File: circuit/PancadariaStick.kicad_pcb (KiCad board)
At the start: 2 copper layers, 64.8 x 63.5 mm, 21 parts, among them CON1 AVR-ISP-10, IC1 ATMEGA8-P, P1 Joystick, P2 Buttons, P3 USB type B, Q1 16MHz

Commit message: Fixed "jumper vias" drill size.
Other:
- net class Default: via_drill 1 -> 0.8
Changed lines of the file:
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@@
     (edge_width 0.15)
     (via_size 2)
-    (via_drill 1)
+    (via_drill 0.8)
     (via_min_size 0.4)
     (via_min_drill 0.3)
@@
       (drillshape 0)
       (scaleselection 1)
-      (outputdirectory curtacircuitos/))
+      (outputdirectory test/))
   )
   (net 0 "")
@@
     (trace_width 0.3)
     (via_dia 2)
-    (via_drill 1)
+    (via_drill 0.8)
     (uvia_dia 0.3)
     (uvia_drill 0.1)

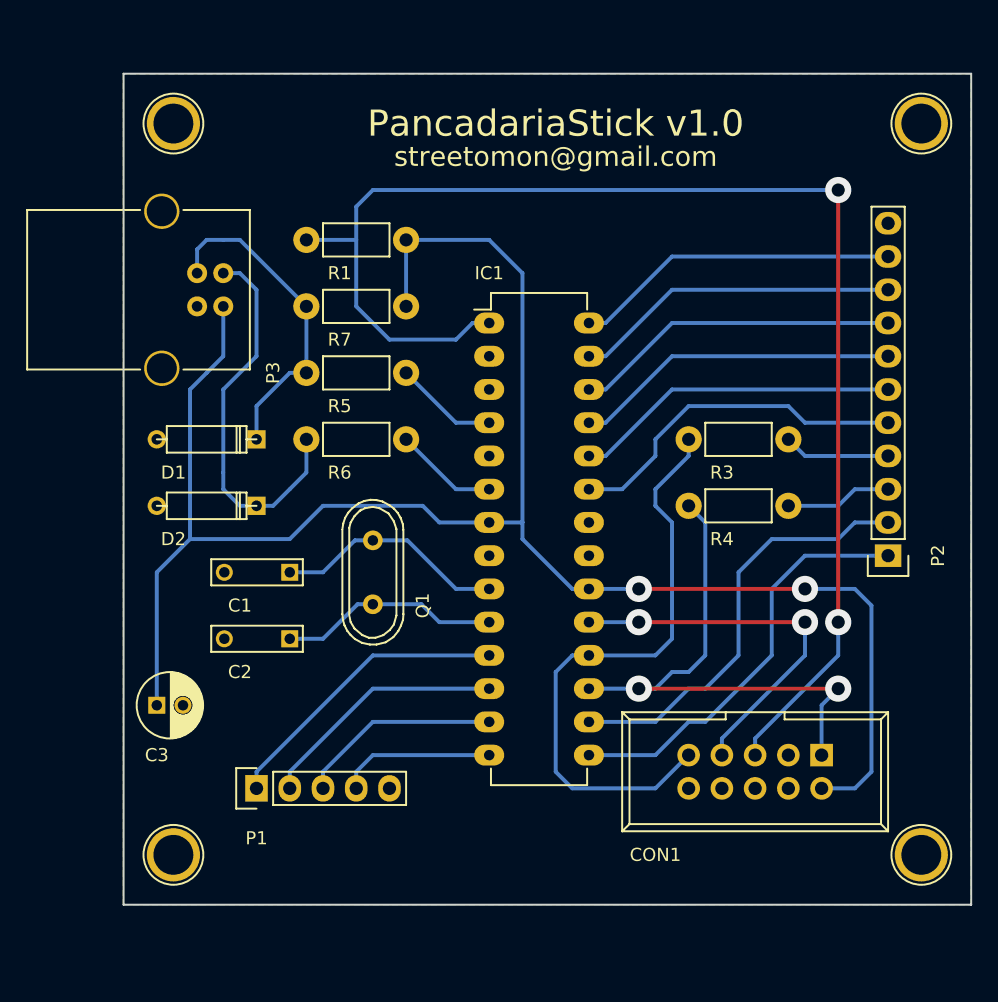
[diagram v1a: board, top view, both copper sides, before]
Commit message: Changed traces width to 0.8 mm.
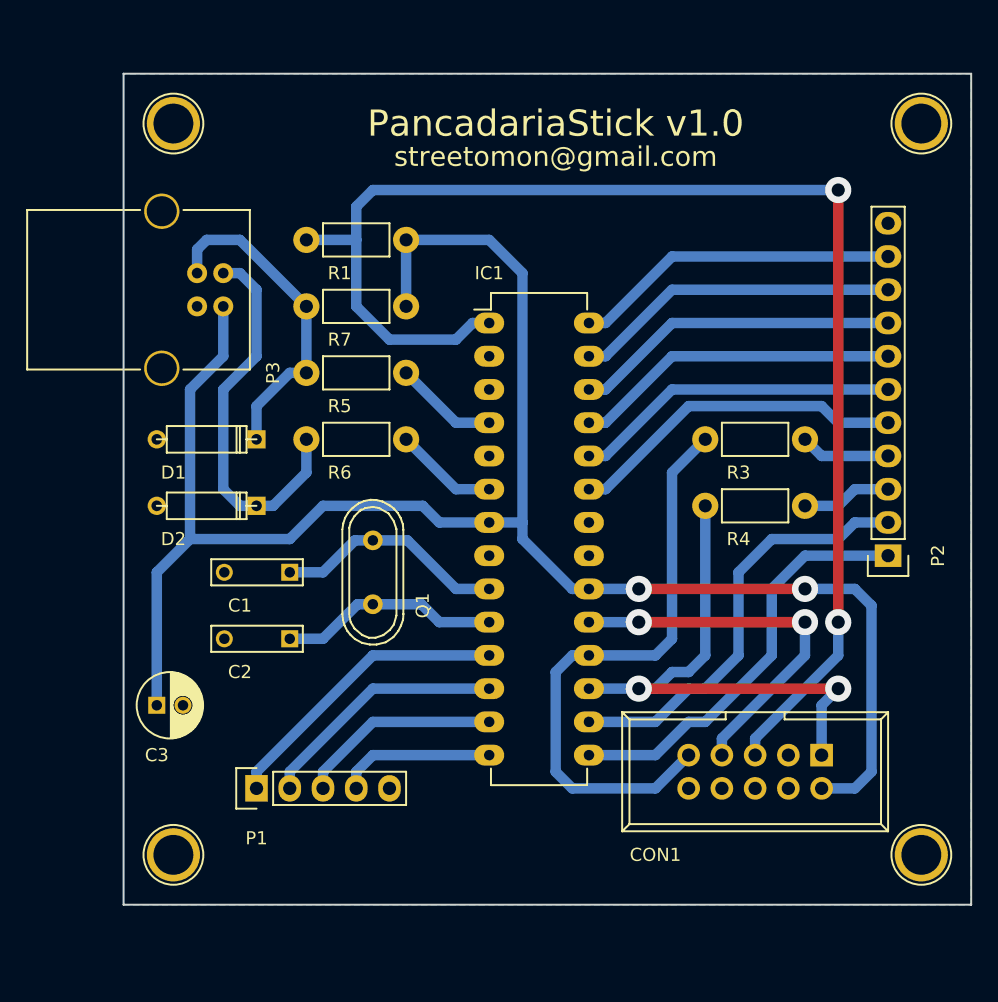
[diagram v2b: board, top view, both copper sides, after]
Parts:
- moved R3 1.27 mm to (137.2, 115.6)
- moved R4 1.27 mm to (137.2, 120.7)
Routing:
- net Net-(P2-Pad4): track 8.15 -> 6.88 mm
- net Net-(P2-Pad3): track 8.15 -> 6.88 mm
- net Net-(IC1-Pad23): track 26.8 -> 26.0 mm
- net Net-(CON1-Pad9): track 46.1 -> 45.6 mm
- net Net-(CON1-Pad1): track 42.7 -> 42.2 mm
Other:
- net class Default: trace_width 0.3 -> 0.8
- rule trace_min: 0.3 -> 0.8

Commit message: Updated board, removed ISP header, changed connectors to block terminals, added LED. Added plots.
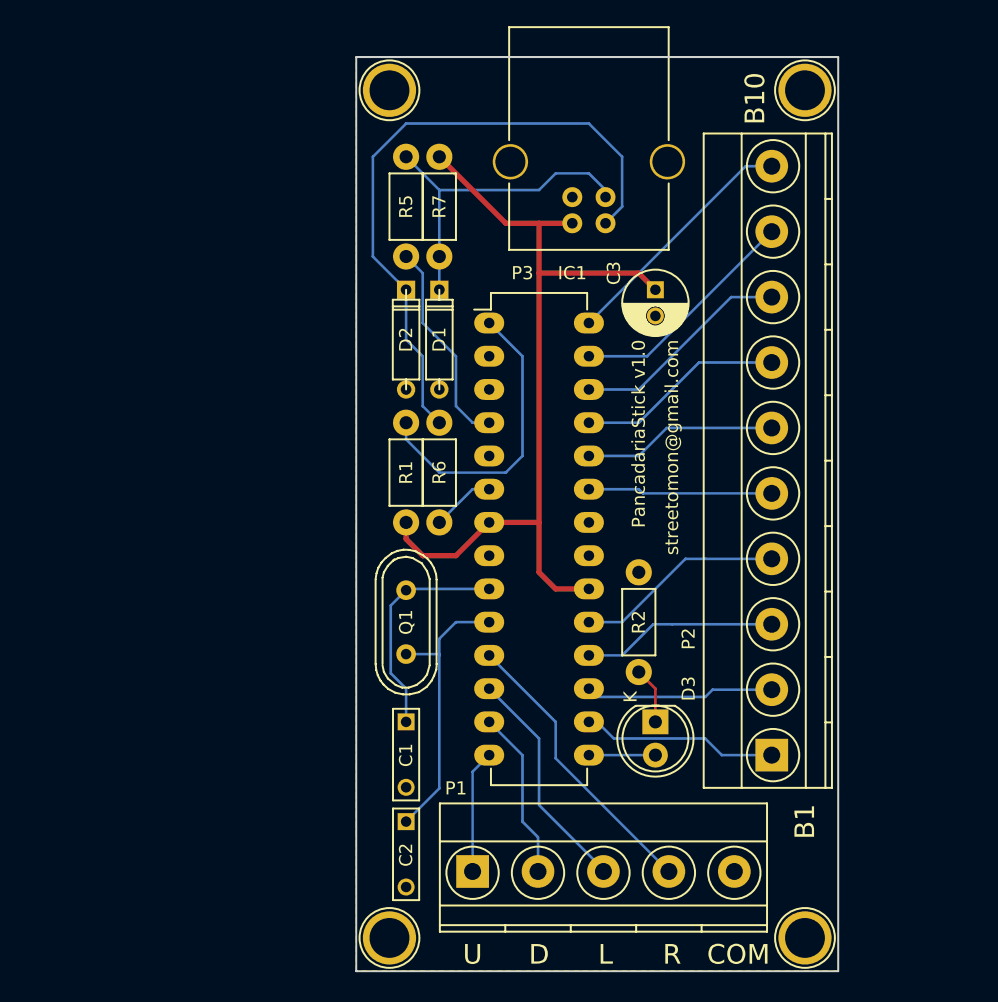
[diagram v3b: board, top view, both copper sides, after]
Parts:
- removed CON1: AVR-ISP-10, Connect:IDC_Header_Straight_10pins
- removed R3, R4: 4k7, Resistors_ThroughHole:Resistor_Horizontal_RM7mm
- removed the REF** at (88.9, 147.3)
- removed the REF** at (88.9, 91.4)
- removed the REF** at (146.1, 147.3)
- removed the REF** at (146.1, 91.4)
- added D3: LED, LEDs:LED-5MM, F.Cu at (125.7, 137.2)
- added R2: 470R, Resistors_ThroughHole:Resistor_Horizontal_RM7mm, F.Cu at (124.5, 133.3)
- added REF**: 1pin, Connect:1pin, F.Cu at (105.4, 88.9)
- added REF**: 1pin, Connect:1pin, F.Cu at (137.2, 88.9)
- added REF**: 1pin, Connect:1pin, F.Cu at (105.4, 153.7)
- added REF**: 1pin, Connect:1pin, F.Cu at (137.2, 153.7)
- P1: footprint Pin_Headers:Pin_Header_Straight_1x05 -> Terminal_Blocks:TerminalBlock_Pheonix_MKDS1.5-5pol
- P2: footprint Pin_Headers:Pin_Header_Straight_1x11 -> Terminal_Blocks:TerminalBlock_Pheonix_MKDS1.5-10pol
- moved C3 49.6 mm to (125.7, 104.1), turned to 270 degrees
- moved P3 27.4 mm to (119.4, 99.1), turned to 90 degrees
- moved D2 19.8 mm to (106.7, 108.0), turned to 90 degrees
- moved D1 19.3 mm to (109.2, 108.0), turned to 90 degrees
- moved R5 18.2 mm to (106.7, 94.0), turned to 270 degrees
- moved P1 17.7 mm to (111.8, 148.6), turned to 0 degrees
- moved P2 17.6 mm to (134.6, 139.7), turned to 90 degrees
- moved C2 16.6 mm to (106.7, 144.8), turned to 270 degrees
- moved R1 15.9 mm to (106.7, 114.3), turned to 270 degrees
- moved C1 14.5 mm to (106.7, 137.2), turned to 270 degrees
- moved R7 11.7 mm to (109.2, 94.0), turned to 270 degrees
- moved R6 10.2 mm to (109.2, 114.3), turned to 270 degrees
- moved Q1 4.58 mm to (106.7, 129.5)
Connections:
- IC1 pad 15: Net-(IC1-Pad15) -> Net-(D3-Pad2)
- IC1 pad 17: Net-(CON1-Pad1) -> Net-(IC1-Pad17)
- IC1 pad 18: Net-(CON1-Pad9) -> Net-(IC1-Pad18)
- IC1 pad 19: Net-(CON1-Pad7) -> Net-(IC1-Pad19)
- P1 pad 1: Net-(IC1-Pad11) -> Net-(IC1-Pad14)
- P1 pad 2: Net-(IC1-Pad12) -> Net-(IC1-Pad13)
- P1 pad 3: Net-(IC1-Pad13) -> Net-(IC1-Pad12)
- P1 pad 4: Net-(IC1-Pad14) -> Net-(IC1-Pad11)
- P2 pad 1: Net-(IC1-Pad15) -> Net-(IC1-Pad16)
- P2 pad 2: Net-(IC1-Pad16) -> Net-(IC1-Pad17)
- P2 pad 3: Net-(P2-Pad3) -> Net-(IC1-Pad18)
- P2 pad 4: Net-(P2-Pad4) -> Net-(IC1-Pad19)
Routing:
- net Net-(IC1-Pad1): track 106.3 -> 23.0 mm, vias 2 -> 0
- net VCC: track 140.7 -> 65.7 mm, vias 2 -> 0
- net Net-(CON1-Pad9): track 45.6 -> 0.00 mm
- net Net-(CON1-Pad1): track 42.2 -> 0.00 mm, vias 2 -> 0
- net Net-(IC1-Pad15): track 32.1 -> 0.00 mm
- net Net-(CON1-Pad7): track 29.3 -> 0.00 mm, vias 2 -> 0
- net Net-(D2-Pad1): track 29.8 -> 49.2 mm
- net Net-(IC1-Pad16): track 32.9 -> 15.0 mm
- net Net-(IC1-Pad19): track 0.00 -> 16.0 mm
- net Net-(IC1-Pad18): track 0.00 -> 15.0 mm
- net Net-(IC1-Pad17): track 0.00 -> 14.5 mm
- net Net-(IC1-Pad23): track 26.0 -> 14.1 mm
- net Net-(IC1-Pad24): track 25.0 -> 14.9 mm
- net Net-(IC1-Pad25): track 25.0 -> 15.9 mm
- net Net-(IC1-Pad4): track 7.93 -> 16.1 mm
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- added copper zone on F.Cu, net GND
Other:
- board size 64.8 x 63.5 mm -> 36.8 x 69.9 mm
- net class Default: trace_width 0.8 -> 0.2; via_dia 2 -> 0.3; via_drill 0.8 -> 0.15
- net class power added: clearance 0.2, trace_width 0.4, via_dia 0.3, via_drill 0.15
- rule trace_min: 0.8 -> 0.2
- rule via_min_drill: 0.3 -> 0.15
- rule via_min_size: 0.4 -> 0.3
- board text added: "B1"
- board text added: "B10"
- board text added: "COM"
- board text added: "D"
- board text added: "L"
- board text added: "R"
- board text added: "U"
